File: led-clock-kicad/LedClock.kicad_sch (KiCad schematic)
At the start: 47 parts, among them J1 Barrel_Jack, J2 AVR-ISP-10, U1 ATmega32-16A, U2 STP16CPC05MTR, U3 STP16CPC05MTR, Y1 Crystal

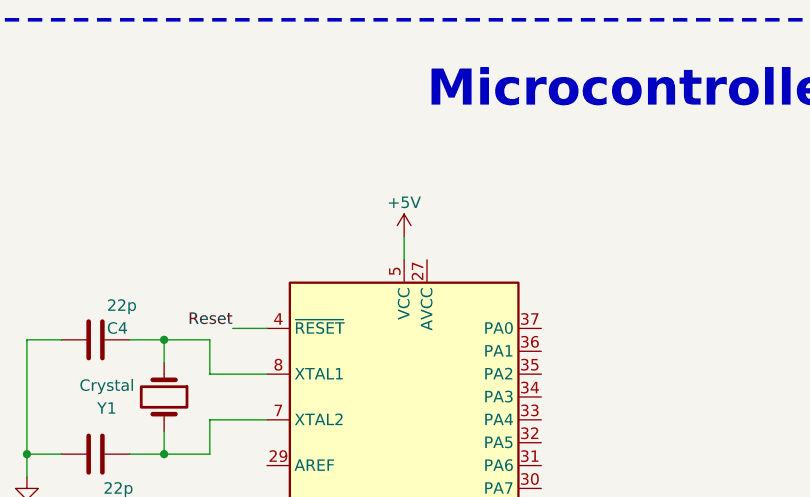
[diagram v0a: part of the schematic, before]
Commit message: Connected AVCC to the 5 volts rail.
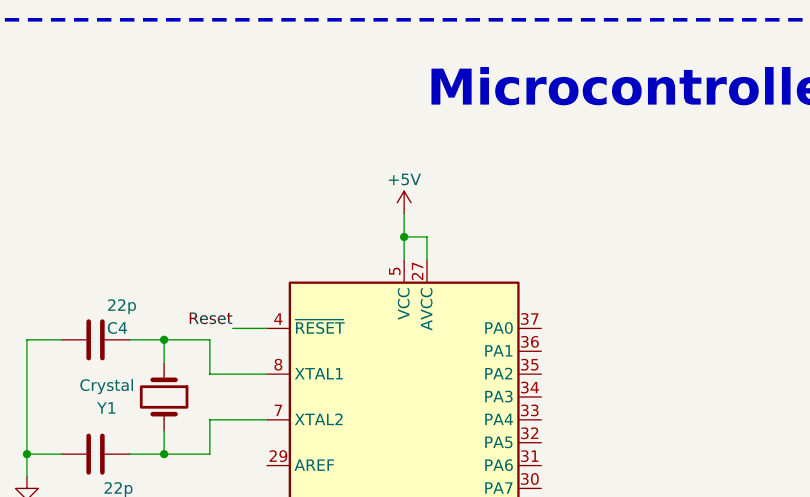
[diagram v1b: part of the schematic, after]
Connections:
- net +5V: now also U1.27 (AVCC)
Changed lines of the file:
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@@
   (junction (at 267.97 41.91) (diameter 0) (color 0 0 0 0)
   )
+  (junction (at 110.49 27.94) (diameter 0) (color 0 0 0 0)
+  )
   (junction (at 267.97 38.1) (diameter 0) (color 0 0 0 0)
   )
@@
     (stroke (width 0) (type default))
   )
+  (wire (pts (xy 110.49 27.94) (xy 110.49 30.48))
+    (stroke (width 0) (type default))
+  )
   (wire (pts (xy 267.97 60.96) (xy 267.97 64.77))
     (stroke (width 0) (type default))
@@
     (stroke (width 0) (type default))
   )
-  (wire (pts (xy 110.49 27.94) (xy 110.49 30.48))
+  (wire (pts (xy 110.49 25.4) (xy 110.49 27.94))
     (stroke (width 0) (type default))
   )
@@
     (stroke (width 0) (type default))
   )
+  (wire (pts (xy 113.03 27.94) (xy 110.49 27.94))
+    (stroke (width 0) (type default))
+  )
   (wire (pts (xy 176.53 185.42) (xy 191.77 185.42))
     (stroke (width 0) (type default))
@@
   )
   (wire (pts (xy 207.01 50.8) (xy 226.06 50.8))
+    (stroke (width 0) (type default))
+  )
+  (wire (pts (xy 113.03 30.48) (xy 113.03 27.94))
     (stroke (width 0) (type default))
   )
@@
     )
   )
-  (symbol (lib_id "power:+5V") (at 110.49 27.94 0) (unit 1)
+  (symbol (lib_id "power:+5V") (at 110.49 25.4 0) (unit 1)
     (in_bom yes) (on_board yes) (dnp no) (fields_autoplaced)
-    (property "Reference" "#PWR03" (at 110.49 31.75 0)
-      (effects (font (size 1.27 1.27)) hide)
-    )
-    (property "Value" "+5V" (at 110.49 24.13 0)
-      (effects (font (size 1.27 1.27)))
-    )
-    (property "Footprint" "" (at 110.49 27.94 0)
-      (effects (font (size 1.27 1.27)) hide)
-    )
-    (property "Datasheet" "" (at 110.49 27.94 0)
-      (effects (font (size 1.27 1.27)) hide)
-    )
+    (property "Reference" "#PWR03" (at 110.49 29.21 0)
+      (effects (font (size 1.27 1.27)) hide)
+    )
+    (property "Value" "+5V" (at 110.49 21.59 0)
+      (effects (font (size 1.27 1.27)))
+    )
+    (property "Footprint" "" (at 110.49 25.4 0)
+      (effects (font (size 1.27 1.27)) hide)
+    )
+    (property "Datasheet" "" (at 110.49 25.4 0)
+      (effects (font (size 1.27 1.27)) hide)
+    )
